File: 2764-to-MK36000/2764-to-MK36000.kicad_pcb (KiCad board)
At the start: 2 copper layers, 22 x 38 mm, 2 parts, among them U1 27C64, U2 MK36000

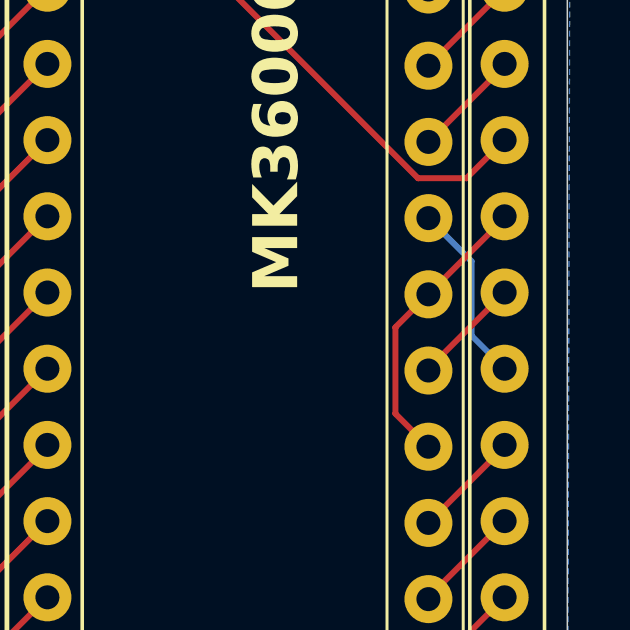
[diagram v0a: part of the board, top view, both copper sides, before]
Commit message: Removed !OE tie to !CE
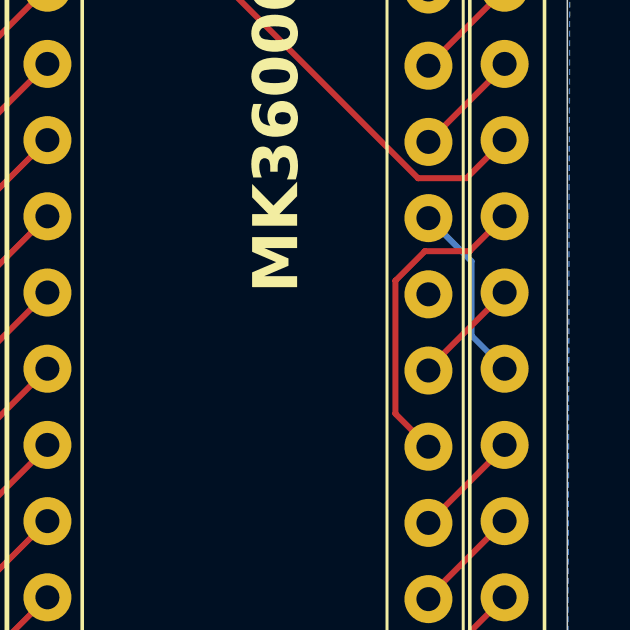
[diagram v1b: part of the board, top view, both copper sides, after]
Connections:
- U1 pad 22: /~{CE} -> unconnected-(U1-~{OE}-Pad22)
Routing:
- net /~{CE}: track 9.64 -> 10.6 mm
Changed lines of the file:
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@@
 	(net 26 "/D_{4}")
 	(net 27 "/A_{9}")
+	(net 28 "unconnected-(U1-~{OE}-Pad22)")
 	(footprint "Package_DIP:DIP-24_W15.24mm_Socket"
 		(layer "F.Cu")
@@
 		)
 		(sheetname "/")
-		(sheetfile "MK36000-to-2764.kicad_sch")
+		(sheetfile "2764-to-MK36000.kicad_sch")
 		(attr through_hole)
 		(fp_line
@@
 		(property ki_fp_filters "DIP*W15.24mm*")
 		(sheetname "/")
-		(sheetfile "MK36000-to-2764.kicad_sch")
+		(sheetfile "2764-to-MK36000.kicad_sch")
 		(attr through_hole)
 		(fp_rect
@@
 			(layers "*.Cu" "*.Mask")
 			(remove_unused_layers no)
-			(net 5 "/~{CE}")
+			(net 28 "unconnected-(U1-~{OE}-Pad22)")
 			(pinfunction "~{OE}")
-			(pintype "input")
+			(pintype "input+no_connect")
 		)
 		(pad "23" thru_hole circle
@@
 	)
 	(segment
+		(start 114.469 84.69395)
+		(end 115.45195 83.711)
+		(width 0.2)
+		(layer "F.Cu")
+		(net 5)
+	)
+	(segment
+		(start 116.949 83.711)
+		(end 118.11 82.55)
+		(width 0.2)
+		(layer "F.Cu")
+		(net 5)
+	)
+	(segment
 		(start 115.57 90.23)
 		(end 114.469 89.129)
@@
 	)
 	(segment
-		(start 115.57 85.15)
-		(end 118.11 82.61)
+		(start 115.45195 83.711)
+		(end 116.949 83.711)
 		(width 0.2)
 		(layer "F.Cu")
@@
 	(segment
 		(start 114.469 89.129)
-		(end 114.469 86.251)
-		(width 0.2)
-		(layer "F.Cu")
-		(net 5)
-	)
-	(segment
-		(start 114.469 86.251)
-		(end 115.57 85.15)
-		(width 0.2)
-		(layer "F.Cu")
+		(end 114.469 84.69395)
+		(width 0.2)
+		(layer "F.Cu")
